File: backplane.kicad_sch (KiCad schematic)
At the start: 0 parts

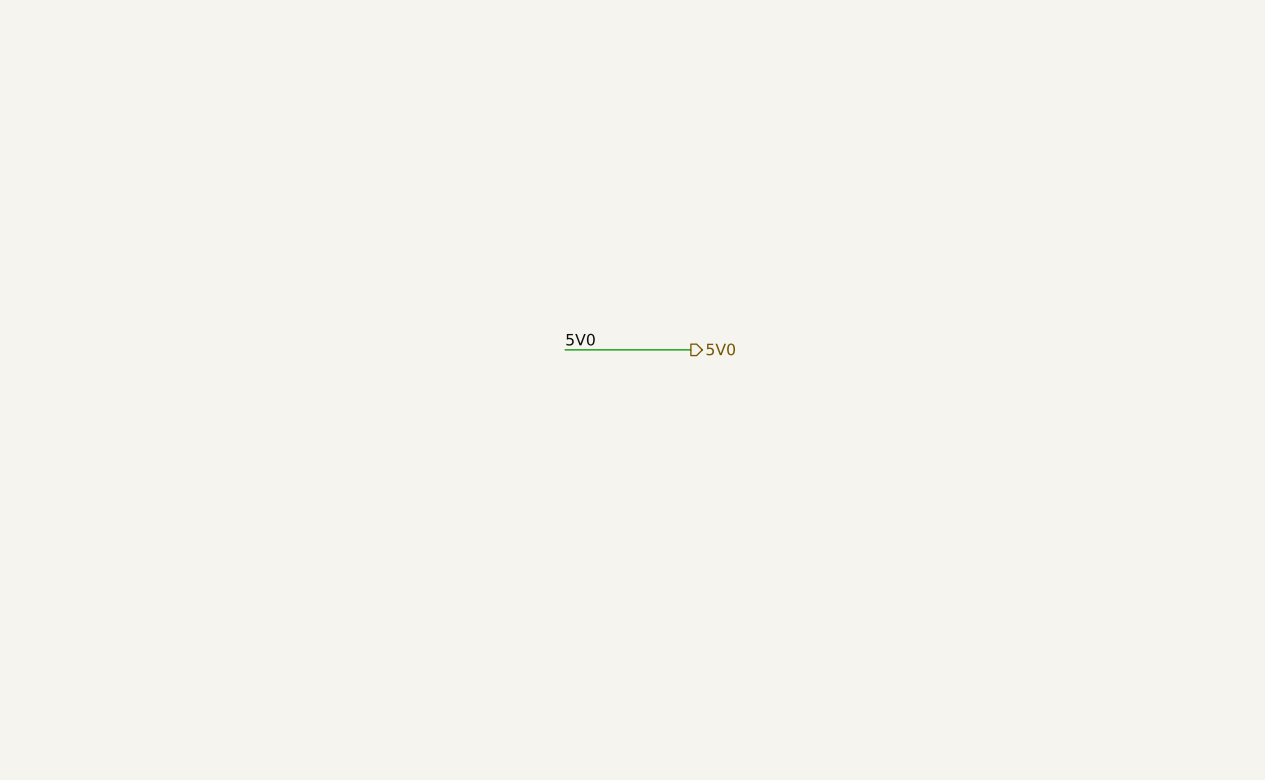
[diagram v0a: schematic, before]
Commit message: added conns to backplane
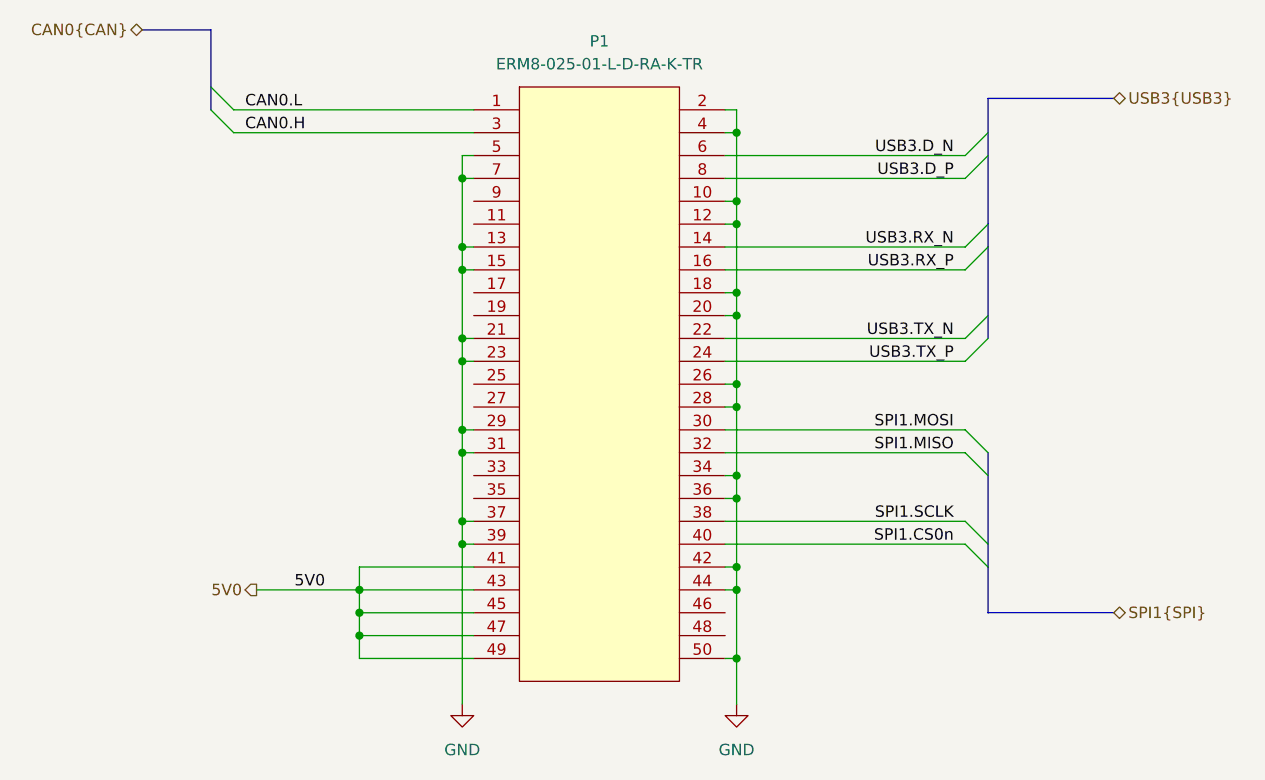
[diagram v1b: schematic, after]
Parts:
- added P1: ERM8-025-01-L-D-RA-K-TR, library:SAMTEC_ERM8-025-XX-X-D-RA-XX, symbol library:ERM8-025-01-L-D-RA-K-TR
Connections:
- net 5V0: now also P1.41, P1.43, P1.45, P1.47, P1.49
- new net CAN0.H: P1.3
- new net CAN0.L: P1.1
- new net GND: P1.10, P1.12, P1.13, P1.15, P1.18, P1.2, P1.20, P1.21, P1.23, P1.26, P1.28, P1.29, P1.31, P1.34, P1.36, P1.37, P1.39, P1.4, P1.42, P1.44, P1.5, P1.50, P1.7
- new net SPI1.CS0n: P1.40
- new net SPI1.MISO: P1.32
- new net SPI1.MOSI: P1.30
- new net SPI1.SCLK: P1.38
- new net USB3.D_N: P1.6
- new net USB3.D_P: P1.8
- new net USB3.RX_N: P1.14
- new net USB3.RX_P: P1.16
- new net USB3.TX_N: P1.22
- new net USB3.TX_P: P1.24

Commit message: finished defining spi/i2c gpio, CAN, off-board signals
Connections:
- net SPI1.CS0n renamed SPI2.CS0n
- net SPI1.MISO renamed SPI2.MISO
- net SPI1.MOSI renamed SPI2.MOSI
- net SPI1.SCLK renamed SPI2.SCLK
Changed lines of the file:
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@@
 		)
 	)
-	(label "SPI1.MISO"
+	(label "SPI2.MISO"
 		(at 181.61 107.95 180)
 		(effects
@@
 		)
 	)
-	(label "SPI1.MOSI"
+	(label "SPI2.MOSI"
 		(at 181.61 105.41 180)
 		(effects
@@
 		)
 	)
-	(label "SPI1.CS0n"
+	(label "SPI2.CS0n"
 		(at 181.61 118.11 180)
 		(effects
@@
 		)
 	)
-	(label "SPI1.SCLK"
+	(label "SPI2.SCLK"
 		(at 181.61 115.57 180)
 		(effects
@@
 		)
 	)
-	(hierarchical_label "SPI1{SPI}"
+	(hierarchical_label "SPI2{SPI}"
 		(shape bidirectional)
 		(at 199.39 125.73 0)

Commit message: starting layout
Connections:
- net CAN0.H: now also P1.03; no longer P1.3
- net CAN0.L: now also P1.01; no longer P1.1
- net GND: now also P1.02, P1.04, P1.05, P1.07; no longer P1.2, P1.4, P1.5, P1.7
- net USB3.D_N: now also P1.06; no longer P1.6
- net USB3.D_P: now also P1.08; no longer P1.8
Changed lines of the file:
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@@
 		(pin "49"
 		)
-		(pin "6"
+		(pin "01"
 		)
 		(pin "45"
 		)
-		(pin "2"
+		(pin "03"
 		)
-		(pin "4"
+		(pin "05"
 		)
 		(pin "41"
@@
 		(pin "35"
 		)
-		(pin "3"
+		(pin "07"
 		)
-		(pin "1"
+		(pin "09"
 		)
 		(pin "33"
@@
 		(pin "11"
 		)
-		(pin "9"
+		(pin "02"
 		)
-		(pin "7"
+		(pin "04"
 		)
-		(pin "5"
+		(pin "06"
 		)
 		(pin "43"
 		)
-		(pin "8"
+		(pin "08"
 		)
 		(pin "10"

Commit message: power planes and sensor placement
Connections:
- net CAN0.H renamed CAN0.P
- net CAN0.L renamed CAN0.N
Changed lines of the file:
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@@
 	)
 	(bus_alias "CAN"
-		(members "H" "L")
+		(members "P" "N")
 	)
 	(junction
@@
 		)
 	)
-	(label "CAN0.L"
+	(label "CAN0.N"
 		(at 102.87 69.85 0)
 		(effects
@@
 		)
 	)
-	(label "CAN0.H"
+	(label "CAN0.P"
 		(at 102.87 72.39 0)
 		(effects

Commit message: redid gpio layout, removed one temp sensor, bom
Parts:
- P1: Manufacturer (none) -> Samtec Inc.; Manufacturer Product Number (none) -> ERM8-025-01-L-D-RA-K-TR
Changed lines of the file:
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@@
+			)
+		)
+		(property "Manufacturer" "Samtec Inc."
+			(at 142.24 100.33 0)
+			(effects
+				(font
+					(size 1.27 1.27)
+				)
+				(hide yes)
+			)
+		)
+		(property "Manufacturer Product Number" "ERM8-025-01-L-D-RA-K-TR"
+			(at 142.24 100.33 0)
+			(effects
+				(font
+					(size 1.27 1.27)
+				)
+				(hide yes)
 			)
 		)
